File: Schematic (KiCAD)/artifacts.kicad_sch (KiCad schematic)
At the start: 40 parts

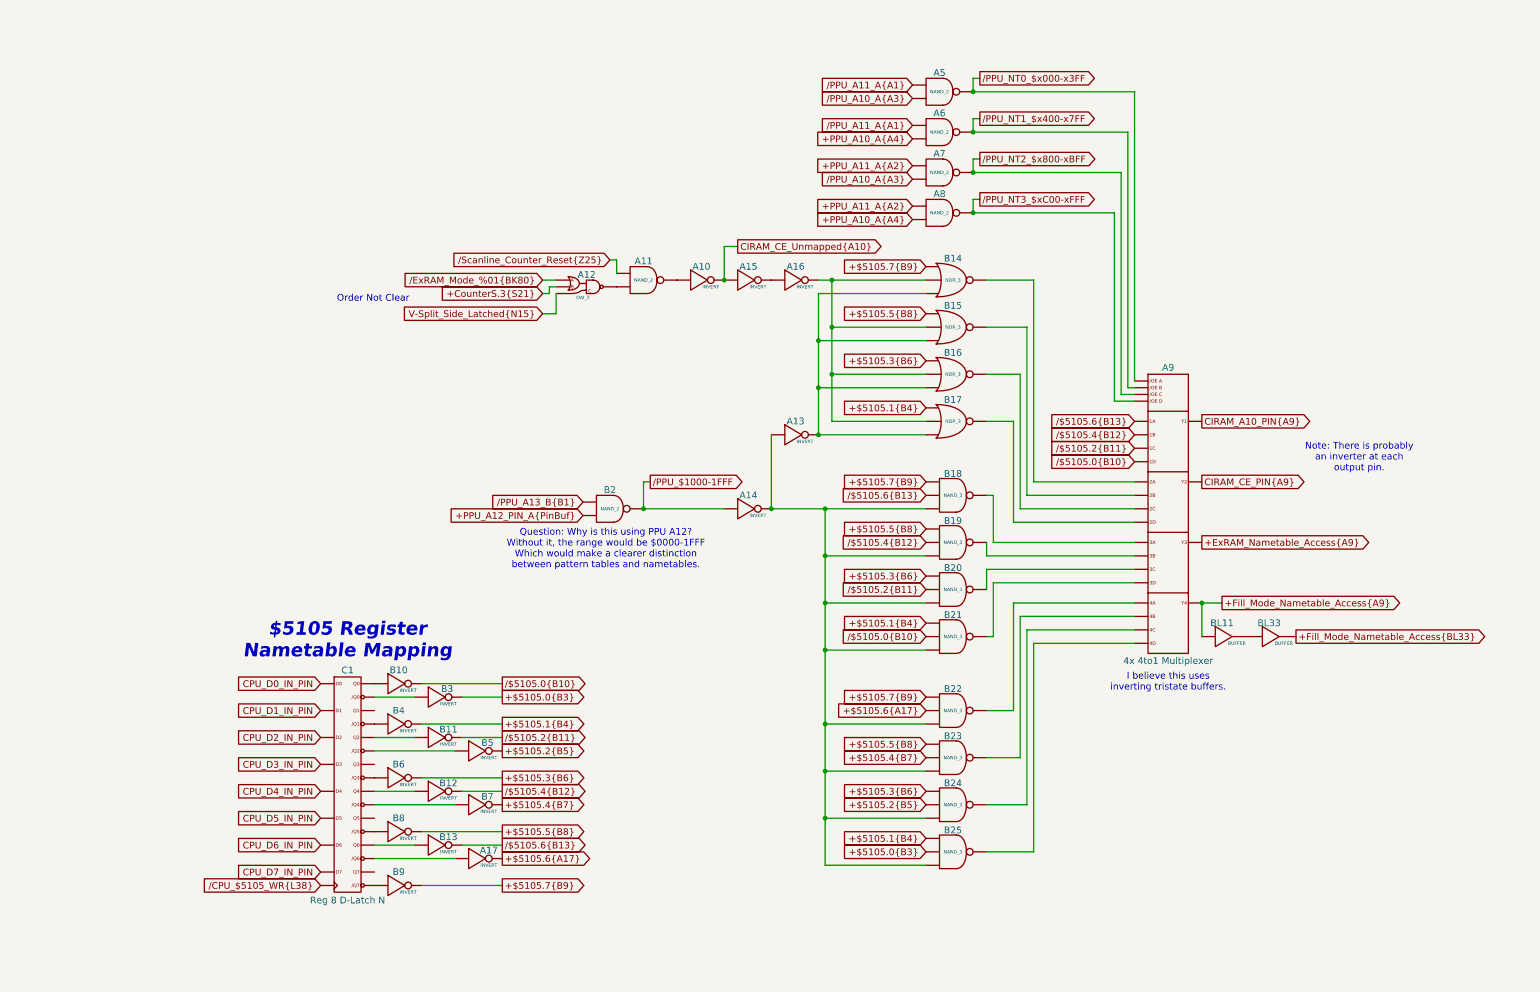
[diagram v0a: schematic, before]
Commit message: - All cells in the left and center areas have now been added into the schematics.  - Changed naming of the PDF files; I was accidentally writing over furrtek's original with my new PDF.
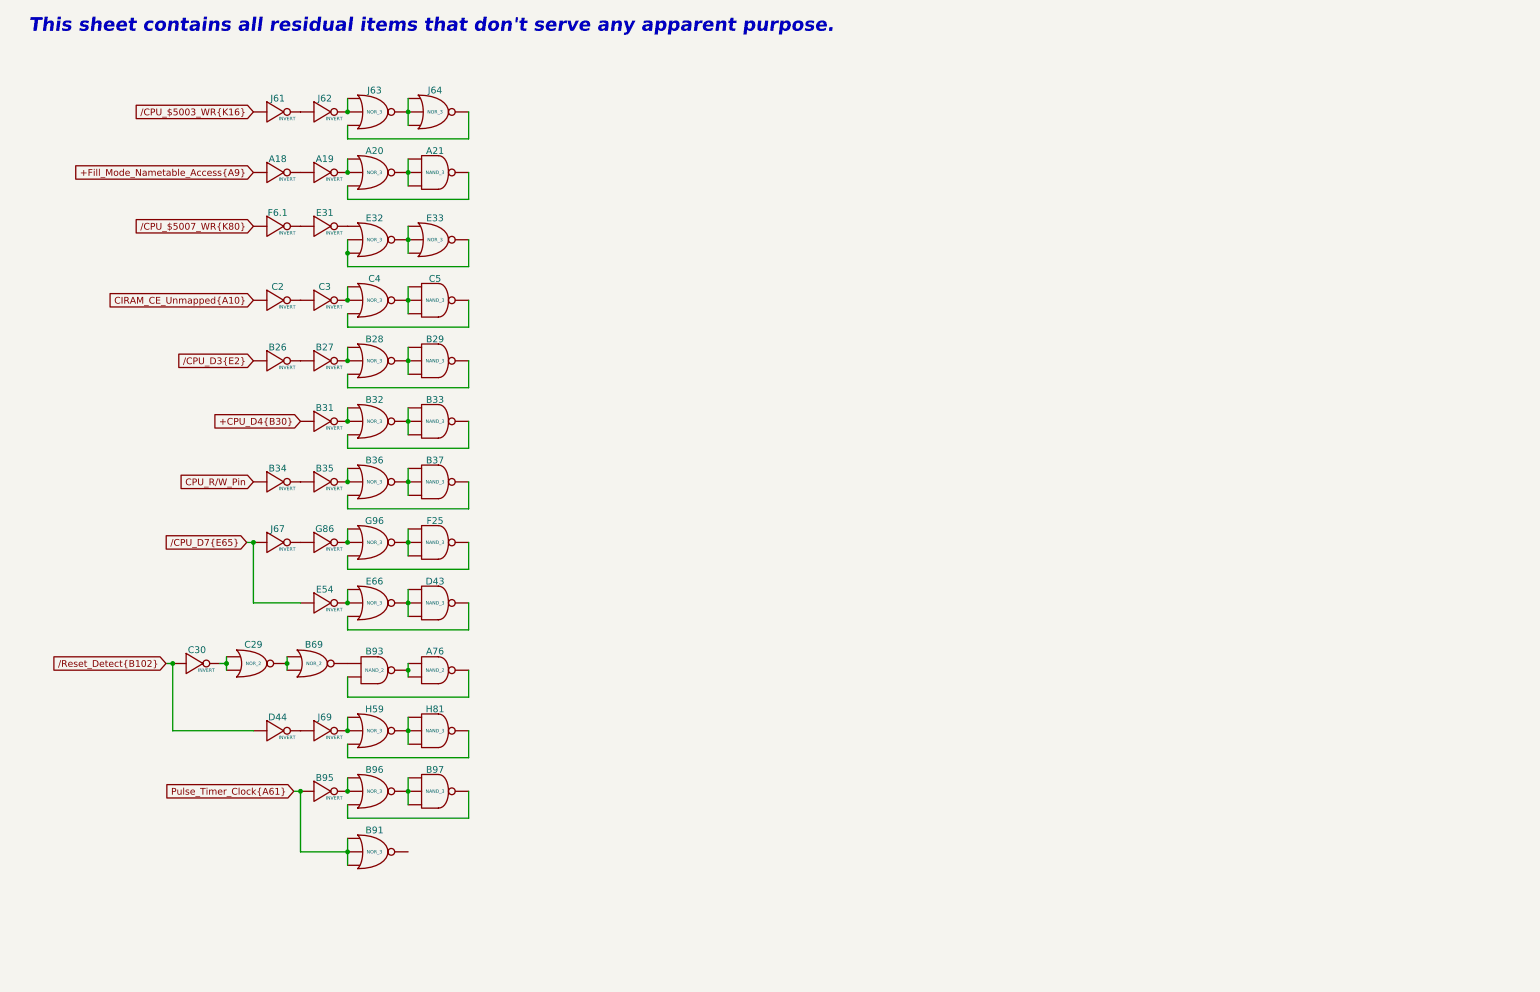
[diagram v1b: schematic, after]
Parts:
- removed A10, A13, A14, A15, A16, A17, B10, B11, B12, B13, B3, B4, B5, B6, B7, B8, B9: INVERT, symbol MMC5:INVERT
- removed A11, A5, A6, A7, A8, B2: NAND_2, symbol MMC5:NAND_2
- removed A12: OAI_2, symbol MMC5:OAI_2
- removed A9: 4x 4to1 Multiplexer, symbol MMC5:Multiplexer_4x4to1
- removed B14, B15, B16, B17: NOR_3, symbol MMC5:NOR_3
- removed B18, B19, B20, B21, B22, B23, B24, B25: NAND_3, symbol MMC5:NAND_3
- removed BL11, BL33: BUFFER, symbol MMC5:BUFFER
- removed C1: Reg 8 D-Latch N, symbol MMC5:Reg_8_D-Latch_N
- added A18, A19, B26, B27, B31, B34, B35, B95, C2, C3, C30, D44, E31, E54, F6.1, G86, J61, J62, J67, J69: INVERT, symbol MMC5:INVERT
- added A20, B28, B32, B36, B91, B96, C4, E32, E33, E66, G96, H59, J63, J64: NOR_3, symbol MMC5:NOR_3
- added A21, B29, B33, B37, B97, C5, D43, F25, H81: NAND_3, symbol MMC5:NAND_3
- added A76, B93: NAND_2, symbol MMC5:NAND_2
- added B69, C29: NOR_2, symbol MMC5:NOR_2
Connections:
- net +Fill_Mode_Nametable_Access{A9}: now also A18. (X)
- net CIRAM_CE_Unmapped{A10}: now also C2. (X)
- new net: J61. (X), J62. (X)
- new net: G86. (X), G96. (X)
- new net: F25. (X), G96. (X) (x2)
- new net: B36. (X), B37. (X) (x2)
- new net: C4. (X), C5. (X) (x2)
- new net: B32. (X), B33. (X) (x2)
- new net: B26. (X), B27. (X)
- new net: A76. (X), B93. (X) (x2)
- new net: H59. (X), H81. (X) (x2)
- new net: A19. (X), A20. (X)
- new net: A20. (X), A21. (X) (x2)
- new net: B96. (X), B97. (X) (x2)
- new net: B31. (X), B32. (X)
- new net: A18. (X), A19. (X)
- new net: E32. (X), E33. (X) (x2)
- new net: G86. (X), J67. (X)
- new net: E31. (X), F6.1. (X)
- new net: E31. (X), E32. (X)
- new net: J62. (X), J63. (X)
- new net: J63. (X), J64. (X) (x2)
- new net: C29. (X), C30. (X)
- new net: C2. (X), C3. (X)
- new net: B69. (X), B93. (X)
- new net: B69. (X), C29. (X)
- new net: B27. (X), B28. (X)
- new net: E54. (X), E66. (X)
- new net: D43. (X), E66. (X) (x2)
- new net: B28. (X), B29. (X) (x2)
- new net: D44. (X), J69. (X)
- new net: H59. (X), J69. (X)
- new net: C3. (X), C4. (X)
- new net: B95. (X), B96. (X)
- new net: B35. (X), B36. (X)
- new net: B34. (X), B35. (X)
- new net +CPU_D4{B30}: B31. (X)
- new net CPU_R/W_Pin: B34. (X)
- new net Pulse_Timer_Clock{A61}: B91. (X), B95. (X)
- new net /CPU_$5003_WR{K16}: J61. (X)
- new net /CPU_$5007_WR{K80}: F6.1. (X)
- new net /CPU_D3{E2}: B26. (X)
- new net /CPU_D7{E65}: E54. (X), J67. (X)
- new net /Reset_Detect{B102}: C30. (X), D44. (X)
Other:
- note added: "This sheet contains all residual items that don't serve any apparent purpose."
- note removed: "$5105 Register Nametable Mapping"
- note removed: "I believe this uses inverting tristate buffers."
- note removed: "Note: There is probably an inverter at each output pin."
- note removed: "Order Not Clear"
- note removed: "Question: Why is this using PPU A12? Without it, the range would be $0000-1FFF Which would make a clearer distinction between pattern tables and nametables."

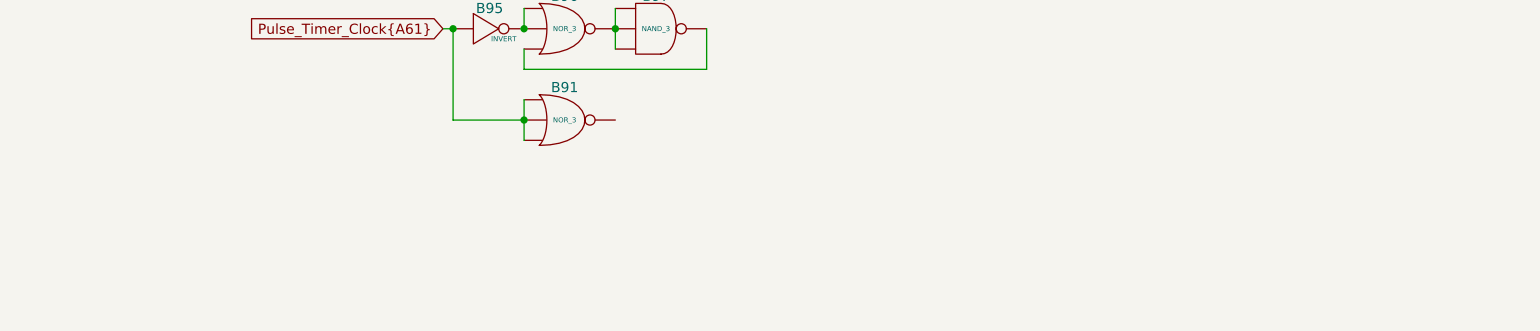
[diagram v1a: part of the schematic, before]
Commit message: - All known gates and traces are now accounted for in the schematics!  :)
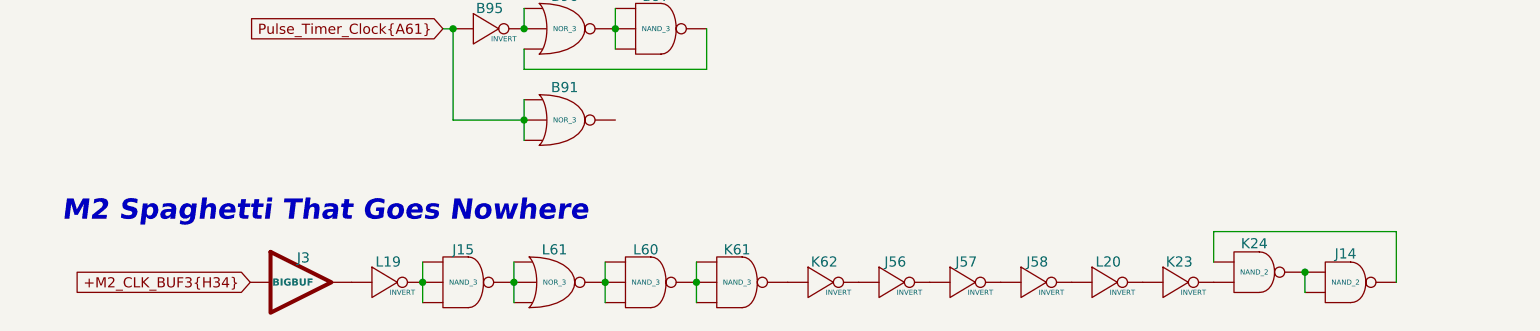
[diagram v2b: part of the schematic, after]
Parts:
- added J14, K24: NAND_2, symbol MMC5:NAND_2
- added J15, K61, L60: NAND_3, symbol MMC5:NAND_3
- added J3: BIGBUF, symbol MMC5:BIGBUF
- added J56, J57, J58, K23, K62, L19, L20: INVERT, symbol MMC5:INVERT
- added L61: NOR_3, symbol MMC5:NOR_3
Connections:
- net at J62. (X): now also J63. (X); no longer J61. (X)
- net at G96. (X): now also F25. (X); no longer G86. (X)
- net at B36. (X): now also B35. (X); no longer B37. (X)
- net at C4. (X): now also C3. (X); no longer C5. (X)
- net at B32. (X): now also B31. (X); no longer B33. (X)
- net at B27. (X): now also B28. (X); no longer B26. (X)
- net at B93. (X): now also B69. (X); no longer A76. (X)
- net at H59. (X): now also J69. (X); no longer H81. (X)
- net at A20. (X): now also A21. (X); no longer A19. (X)
- net at B96. (X): now also B95. (X); no longer B97. (X)
- net at E32. (X): now also E31. (X); no longer E33. (X)
- net at J63. (X): now also J64. (X); no longer J62. (X)
- net at C29. (X): now also B69. (X); no longer C30. (X)
- net at B28. (X): now also B29. (X); no longer B27. (X)
- net at E66. (X): now also D43. (X); no longer E54. (X)
- net at B35. (X): now also B34. (X); no longer B36. (X)
- new net: L60. (X), L61. (X)
- new net: J15. (X), L61. (X)
- new net: J61. (X), J62. (X)
- new net: G86. (X), G96. (X)
- new net: F25. (X), G96. (X)
- new net: B36. (X), B37. (X)
- new net: C4. (X), C5. (X)
- new net: B32. (X), B33. (X)
- new net: B26. (X), B27. (X)
- new net: K23. (X), L20. (X)
- new net: J58. (X), L20. (X)
- new net: A76. (X), B93. (X)
- new net: H59. (X), H81. (X)
- new net: J56. (X), J57. (X)
- new net: J56. (X), K62. (X)
- new net: A19. (X), A20. (X)
- new net: A20. (X), A21. (X)
- new net: B96. (X), B97. (X)
- new net: K61. (X), L60. (X)
- new net: E32. (X), E33. (X)
- new net: E31. (X), F6.1. (X)
- new net: J63. (X), J64. (X)
- new net: J3. (X), L19. (X)
- new net: J15. (X), L19. (X)
- new net: C29. (X), C30. (X)
- new net: C2. (X), C3. (X)
- new net: J57. (X), J58. (X)
- new net: K61. (X), K62. (X)
- new net: E54. (X), E66. (X)
- new net: D43. (X), E66. (X)
- new net: J14. (X), K24. (X) (x2)
- new net: B28. (X), B29. (X)
- new net: K23. (X), K24. (X)
- new net: D44. (X), J69. (X)
- new net +M2_CLK_BUF3{H34}: J3. (X)
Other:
- note added: "M2 Spaghetti That Goes Nowhere"
